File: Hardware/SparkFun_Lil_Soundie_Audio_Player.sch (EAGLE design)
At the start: 65 parts, among them J1 Audio Jack, J2 AMP FCI 10103594-0001LF, U2 VS1000, U3 4MB Flash, Y1 12MHz

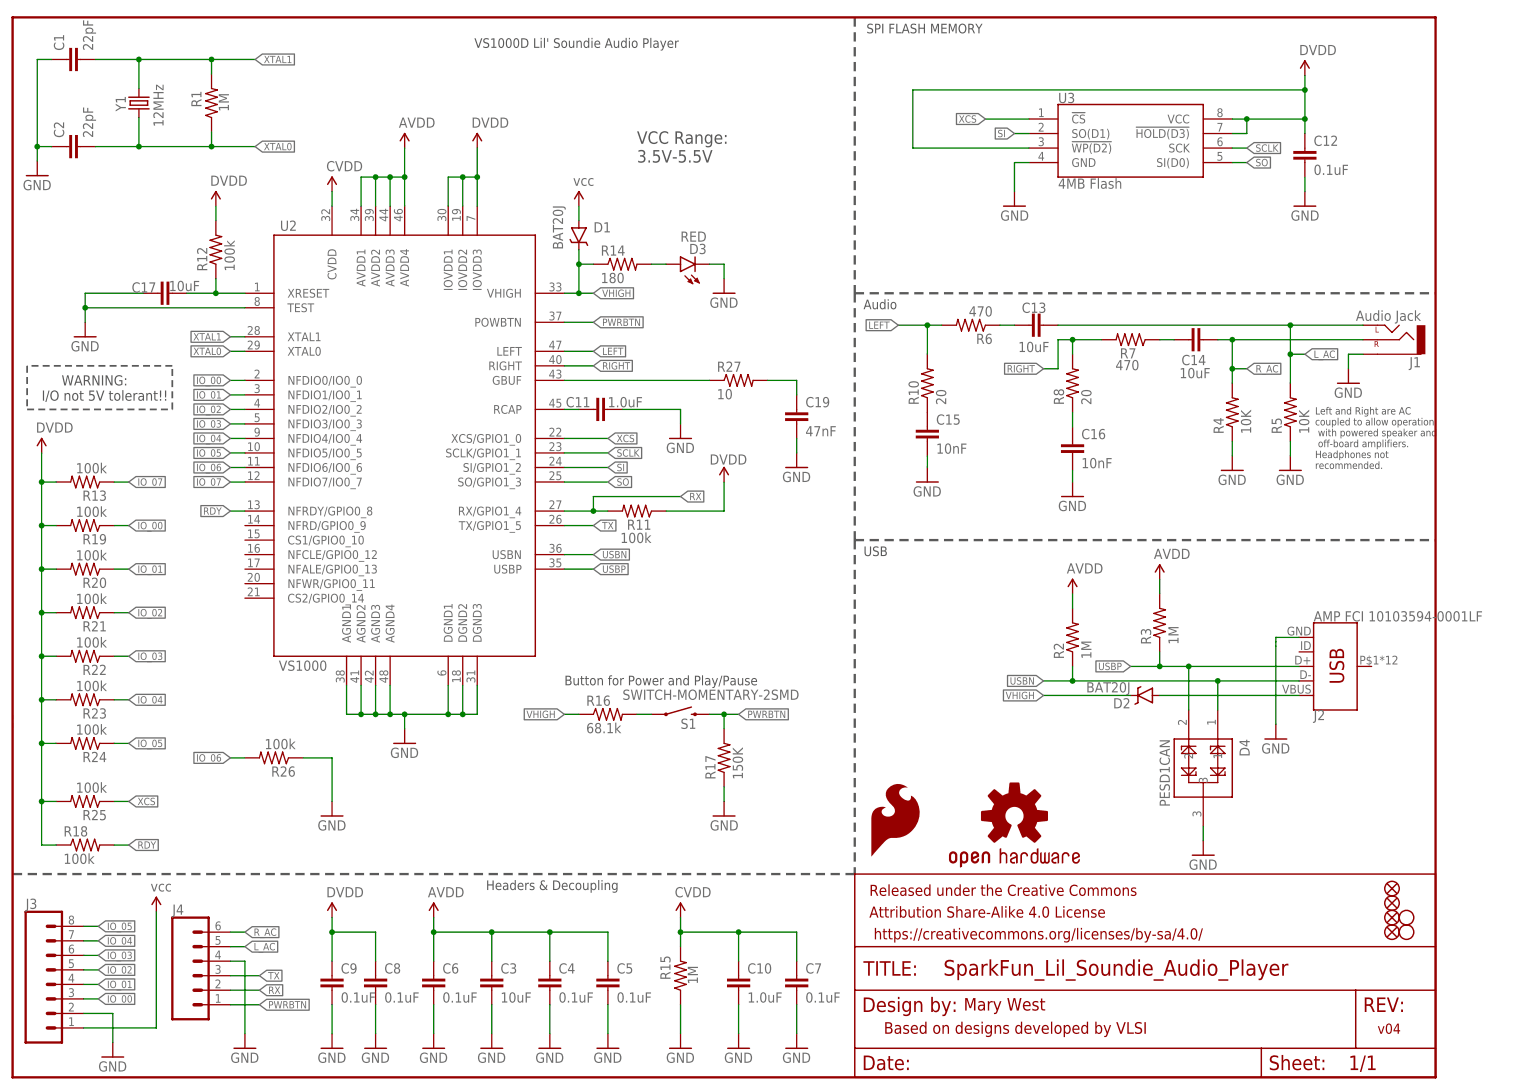
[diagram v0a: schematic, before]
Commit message: Updated design: active high input pins. Cleaned up schematic and layout
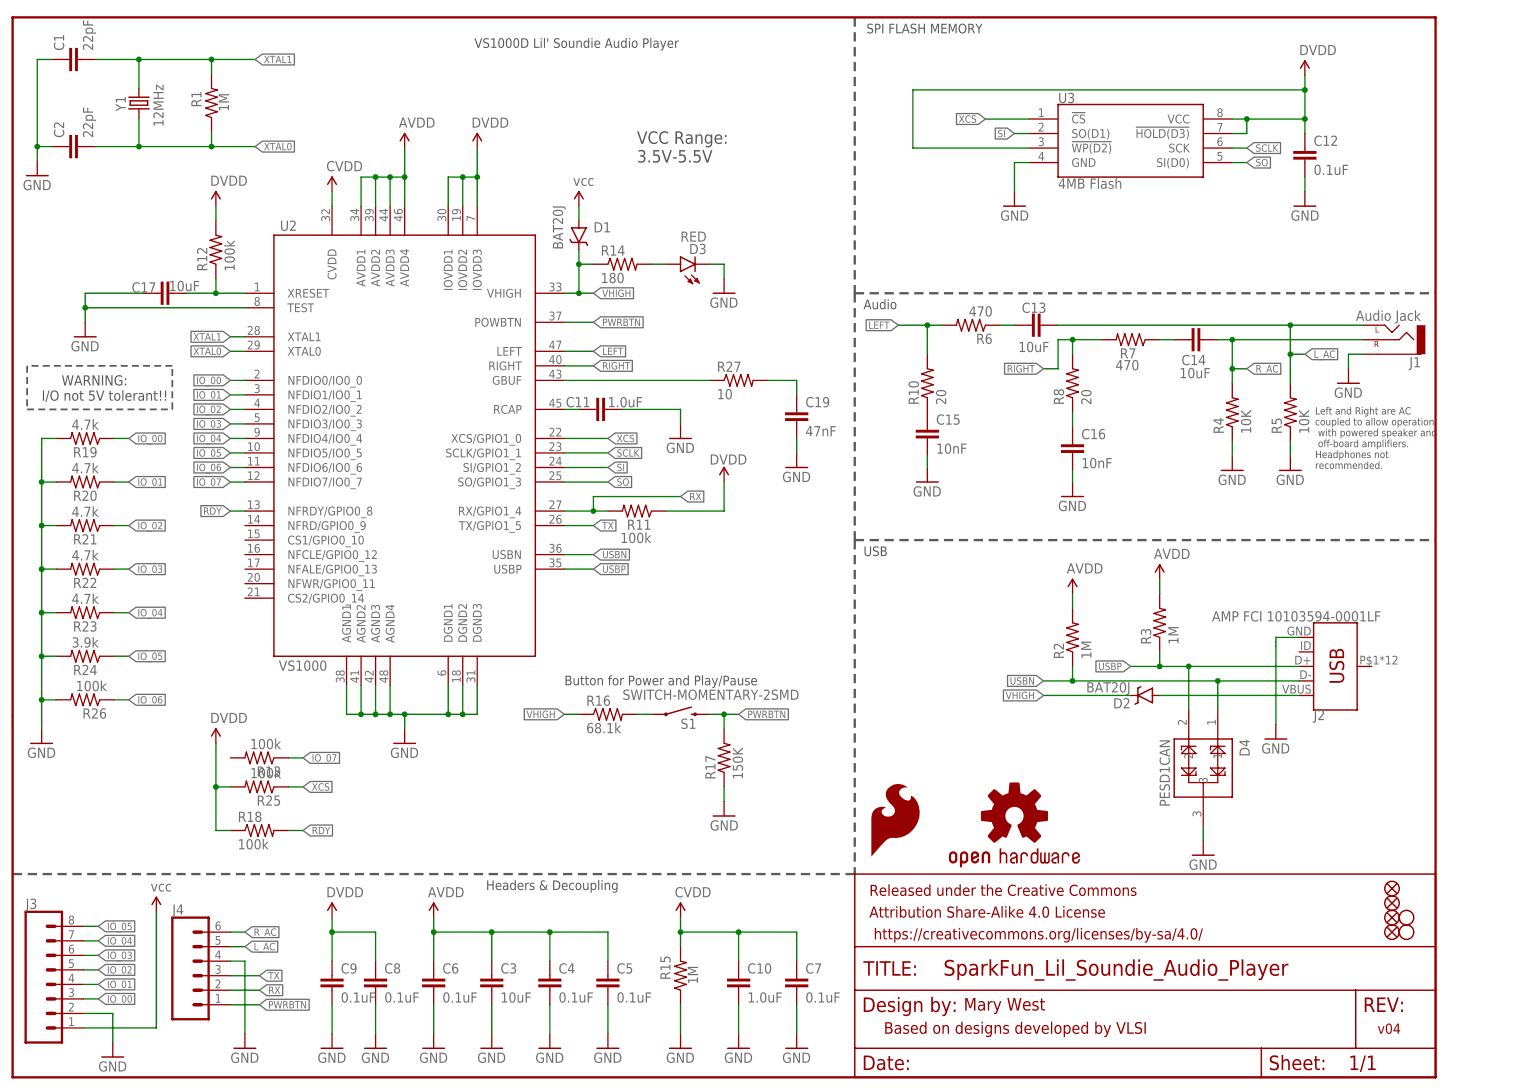
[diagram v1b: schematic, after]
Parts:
- R19, R20, R21, R22, R23: value 100k -> 4.7k; device SparkFun-Resistors:100KOHM-1/10W-1%(0603) -> SparkFun-Resistors:4.7KOHM-0603-1/10W-1%
- R24: value 100k -> 3.9k; device SparkFun-Resistors:100KOHM-1/10W-1%(0603) -> SparkFun-Resistors:3.9KOHM-0603-1/10W-1%
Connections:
- net DVDD: no longer R13.2, R19.2, R20.2, R21.2, R22.2, R23.2, R24.2
- net GND: now also R19.2, R20.2, R21.2, R22.2, R23.2, R24.2, R26.2; no longer R26.1
- net IO_06: now also R26.1; no longer R26.2
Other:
- moved on the sheet: R13, R18, R19, R20, R21, R22, R23, R24, R25, R26

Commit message: Fixed trace issue on IO7
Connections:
- net DVDD: now also R13.2
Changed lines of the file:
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@@
 <segment>
 <pinref part="SUPPLY9" gate="G$1" pin="VCC"/>
-<wire x1="35.56" y1="58.42" x2="35.56" y2="50.8" width="0.1524" layer="91"/>
+<wire x1="35.56" y1="58.42" x2="35.56" y2="55.88" width="0.1524" layer="91"/>
 <pinref part="R25" gate="G$1" pin="2"/>
+<wire x1="35.56" y1="55.88" x2="35.56" y2="50.8" width="0.1524" layer="91"/>
 <wire x1="35.56" y1="50.8" x2="38.1" y2="50.8" width="0.1524" layer="91"/>
 <pinref part="R18" gate="G$1" pin="1"/>
@@
 <wire x1="35.56" y1="43.18" x2="35.56" y2="50.8" width="0.1524" layer="91"/>
 <junction x="35.56" y="50.8"/>
+<pinref part="R13" gate="G$1" pin="2"/>
+<wire x1="38.1" y1="55.88" x2="35.56" y2="55.88" width="0.1524" layer="91"/>
+<junction x="35.56" y="55.88"/>
 </segment>
 <segment>

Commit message: Updated per QC review
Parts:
- D1, D2: value BAT20J -> 1A/23V/620mV
- U2: value VS1000 -> VS1000D; device SparkFun-DigitalIC:VS1000 -> SparkFun-IC-Conversion:VS1000; PROD_ID IC-08955 -> LPA-12743
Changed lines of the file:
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@@
 <parts>
 <part name="FRAME1" library="SparkFun-Aesthetics" deviceset="FRAME-LETTER" device=""/>
-<part name="U2" library="SparkFun-DigitalIC" deviceset="VS1000" device="">
-<attribute name="PROD_ID" value="IC-08955"/>
+<part name="U2" library="SparkFun-IC-Conversion" deviceset="VS1000" device="" value="VS1000D">
+<attribute name="PROD_ID" value="LPA-12743"/>
 </part>
 <part name="LOGO1" library="SparkFun-Aesthetics" deviceset="OSHW-LOGO" device="L" value="OSHW-LOGOL"/>
@@
 <part name="R17" library="SparkFun-Resistors" deviceset="150KOHM1/10W1%(0603)" device="" value="150K"/>
 <part name="GND22" library="SparkFun-Aesthetics" deviceset="GND" device=""/>
-<part name="D1" library="SparkFun-DiscreteSemi" deviceset="DIODE-SCHOTTKY" device="-BAT20J" value="BAT20J"/>
-<part name="D2" library="SparkFun-DiscreteSemi" deviceset="DIODE-SCHOTTKY" device="-BAT20J" value="BAT20J"/>
+<part name="D1" library="SparkFun-DiscreteSemi" deviceset="DIODE-SCHOTTKY" device="-BAT20J" value="1A/23V/620mV"/>
+<part name="D2" library="SparkFun-DiscreteSemi" deviceset="DIODE-SCHOTTKY" device="-BAT20J" value="1A/23V/620mV"/>
 <part name="D3" library="SparkFun-LED" deviceset="LED-RED" device="0603" value="RED"/>
 <part name="GND23" library="SparkFun-Aesthetics" deviceset="GND" device=""/>
@@
 </instance>
 <instance part="GND25" gate="1" x="160.02" y="104.14"/>
-<instance part="D4" gate="G$1" x="203.2" y="59.182" rot="R270"/>
+<instance part="D4" gate="G$1" x="208.28" y="59.182" rot="R270"/>
 <instance part="GND28" gate="1" x="208.28" y="38.862"/>
 <instance part="R8" gate="G$1" x="185.42" y="121.412" rot="R90"/>
@@
 <pinref part="D4" gate="G$1" pin="3"/>
 <pinref part="GND28" gate="1" pin="GND"/>
-<wire x1="208.28" y1="43.942" x2="208.28" y2="41.402" width="0.1524" layer="91"/>
+<wire x1="208.28" y1="51.562" x2="208.28" y2="41.402" width="0.1524" layer="91"/>
 </segment>
 <segment>
@@
 <junction x="185.42" y="69.342"/>
 <pinref part="D4" gate="G$1" pin="1"/>
-<wire x1="210.82" y1="64.262" x2="210.82" y2="69.342" width="0.1524" layer="91"/>
+<wire x1="210.82" y1="66.802" x2="210.82" y2="69.342" width="0.1524" layer="91"/>
 <junction x="210.82" y="69.342"/>
 </segment>
@@
 <label x="195.58" y="71.882" size="1.27" layer="95" rot="R180" xref="yes"/>
 <pinref part="D4" gate="G$1" pin="2"/>
-<wire x1="205.74" y1="64.262" x2="205.74" y2="71.882" width="0.1524" layer="91"/>
+<wire x1="205.74" y1="66.802" x2="205.74" y2="71.882" width="0.1524" layer="91"/>
 <junction x="205.74" y="71.882"/>
 </segment>

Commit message: Updating Silk
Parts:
- removed R16: 68.1k, SparkFun-Resistors:68.1KOHM1/10W1%(0603)
- LOGO2: value SFE_LOGO_FLAME.4_INCH -> SFE_LOGO_NAME.1_INCH; device SparkFun-Aesthetics:SFE_LOGO_FLAME.4_INCH -> SparkFun-Aesthetics:SFE_LOGO_NAME.1_INCH
- R19, R20, R21, R22, R23: value 4.7k -> 100k; device SparkFun-Resistors:4.7KOHM-0603-1/10W-1% -> SparkFun-Resistors:100KOHM-0603-1/10W-1%
- R24: value 3.9k -> 100k; device SparkFun-Resistors:3.9KOHM-0603-1/10W-1% -> SparkFun-Resistors:100KOHM-0603-1/10W-1%
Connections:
- removed net N$16: R16.2, S1.1
- new net N$8: R11.1
- net DVDD: now also R11.2; no longer R11.1
- net RX: no longer R11.2
- net VHIGH: now also S1.1; no longer R16.1
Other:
- note added: "Audio Out"
- note added: "Lil' Soundie Audio Breakout Board"
- note added: "POWER TO VS1000D"
- note added: "v10"
- note removed: "Audio"
- note removed: "Button for Power and Play/Pause"
- note removed: "VS1000D Lil' Soundie Audio Player"
- note removed: "v04"
- moved on the sheet: C19, R11, R17, R19, R20, R21, R22, R23, R24, R26, R27, S1

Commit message: Updated name
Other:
- note added: "Little Soundie Audio Breakout Board"
- note removed: "Lil' Soundie Audio Breakout Board"
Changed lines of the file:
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@@
 <text x="151.384" y="86.106" size="3.048" layer="97" font="vector">USB</text>
 <text x="150.114" y="138.43" size="3.048" layer="97" font="vector">Audio Out</text>
-<text x="103.632" y="177.546" size="3.81" layer="97" font="vector" align="center"> Lil' Soundie
+<text x="103.632" y="177.546" size="3.81" layer="97" font="vector" align="center"> Little Soundie
 Audio Breakout Board</text>
 <wire x1="2.54" y1="121.92" x2="2.54" y2="114.3" width="0.3048" layer="97" style="shortdash"/>
